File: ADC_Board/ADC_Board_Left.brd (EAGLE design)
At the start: 63.5 x 81.3 mm, 24 parts

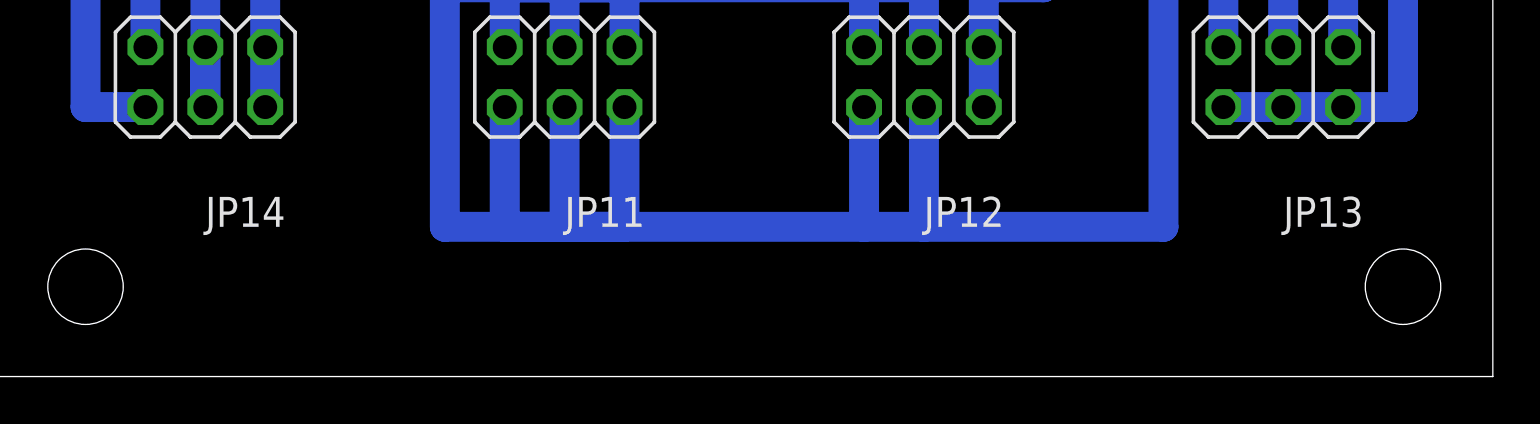
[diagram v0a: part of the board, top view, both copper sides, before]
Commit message: Alterações ligeiras nos esquemas eléctricos das placas das ADCs.
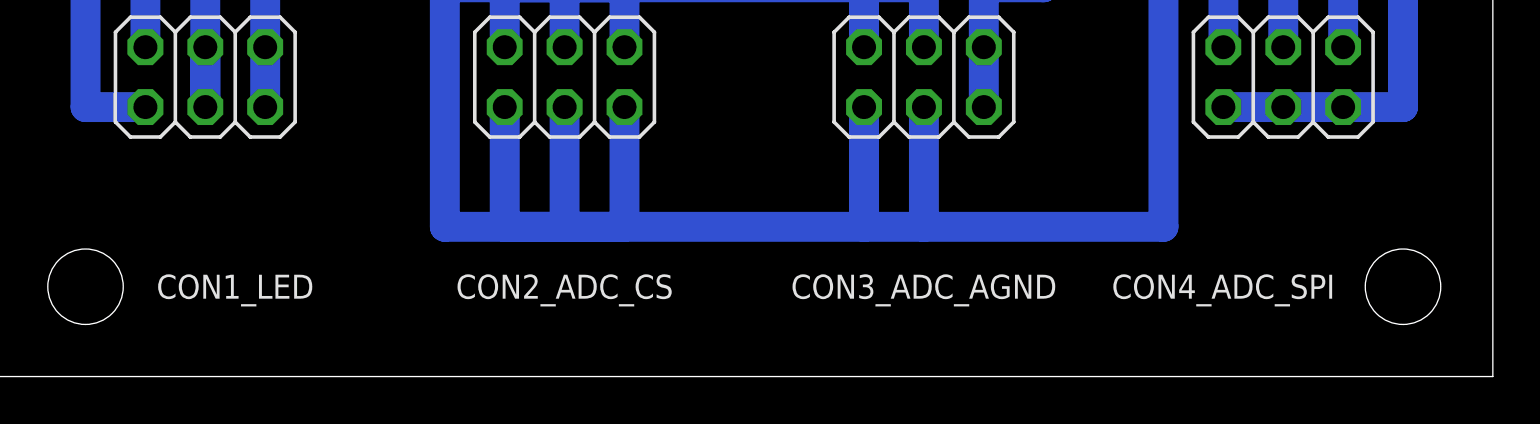
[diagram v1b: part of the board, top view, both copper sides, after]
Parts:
- renumbered JP11 to CON2_ADC_CS, JP12 to CON3_ADC_AGND, JP13 to CON4_ADC_SPI, JP14 to CON1_LED
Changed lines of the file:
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@@
 <wire x1="63.5" y1="-81.28" x2="0" y2="-81.28" width="0" layer="20"/>
 <text x="45.72" y="-12.7" size="1.778" layer="51">LEFT BOARD</text>
-<text x="-22.86" y="-12.7" size="1.778" layer="51">RIGHT CABLES</text>
+<text x="68.58" y="-12.7" size="1.778" layer="51">RIGHT CABLES</text>
 <text x="6.35" y="-64.77" size="1.016" layer="51" align="center">DI</text>
 <text x="6.35" y="-72.39" size="1.016" layer="51" align="center">DO</text>
@@
 <element name="JP9" library="pinhead" package="1X06" value="" x="29.21" y="-53.34" rot="R270"/>
 <element name="JP10" library="pinhead" package="1X06" value="" x="34.29" y="-53.34" rot="R270"/>
-<element name="JP11" library="pinhead" package="2X03" value="" x="24.13" y="-68.58" smashed="yes">
-<attribute name="NAME" x="24.13" y="-74.93" size="1.27" layer="25" ratio="10"/>
+<element name="CON2_ADC_CS" library="pinhead" package="2X03" value="" x="24.13" y="-68.58" smashed="yes">
+<attribute name="NAME" x="24.13" y="-77.47" size="1.016" layer="25" ratio="10" align="center"/>
 <attribute name="VALUE" x="20.32" y="-73.025" size="1.27" layer="27"/>
 </element>
-<element name="JP12" library="pinhead" package="2X03" value="" x="39.37" y="-68.58" smashed="yes">
-<attribute name="NAME" x="39.37" y="-74.93" size="1.27" layer="25" ratio="10"/>
+<element name="CON3_ADC_AGND" library="pinhead" package="2X03" value="" x="39.37" y="-68.58" smashed="yes">
+<attribute name="NAME" x="39.37" y="-77.47" size="1.016" layer="25" ratio="10" align="center"/>
 <attribute name="VALUE" x="35.56" y="-73.025" size="1.27" layer="27"/>
 </element>
-<element name="JP13" library="pinhead" package="2X03" value="" x="54.61" y="-68.58" smashed="yes">
-<attribute name="NAME" x="54.61" y="-74.93" size="1.27" layer="25" ratio="10"/>
+<element name="CON4_ADC_SPI" library="pinhead" package="2X03" value="" x="54.61" y="-68.58" smashed="yes">
+<attribute name="NAME" x="52.07" y="-77.47" size="1.016" layer="25" ratio="10" align="center"/>
 <attribute name="VALUE" x="50.8" y="-73.025" size="1.27" layer="27"/>
 </element>
-<element name="JP14" library="pinhead" package="2X03" value="" x="8.89" y="-68.58" smashed="yes">
-<attribute name="NAME" x="8.89" y="-74.93" size="1.27" layer="25" ratio="10"/>
+<element name="CON1_LED" library="pinhead" package="2X03" value="" x="8.89" y="-68.58" smashed="yes">
+<attribute name="NAME" x="10.16" y="-77.47" size="1.016" layer="25" ratio="10" align="center"/>
 <attribute name="VALUE" x="5.08" y="-73.025" size="1.27" layer="27"/>
 </element>
@@
 </signal>
 <signal name="GND">
-<contactref element="JP14" pad="5"/>
-<contactref element="JP14" pad="6"/>
+<contactref element="CON1_LED" pad="5"/>
+<contactref element="CON1_LED" pad="6"/>
 <wire x1="11.43" y1="-69.85" x2="11.43" y2="-67.31" width="1.27" layer="16"/>
 <wire x1="19.05" y1="-59.69" x2="11.43" y2="-59.69" width="1.27" layer="16"/>
@@
 <wire x1="13.97" y1="-49.53" x2="34.29" y2="-49.53" width="1.27" layer="16"/>
 <wire x1="8.89" y1="-49.53" x2="8.89" y2="-52.07" width="1.27" layer="16"/>
-<contactref element="JP14" pad="3"/>
-<contactref element="JP14" pad="4"/>
+<contactref element="CON1_LED" pad="3"/>
+<contactref element="CON1_LED" pad="4"/>
 <via x="8.89" y="-52.07" extent="1-16" drill="0.6" shape="square"/>
 <wire x1="8.89" y1="-52.07" x2="8.89" y2="-57.15" width="1.27" layer="1"/>
@@
 <wire x1="46.99" y1="-36.83" x2="52.07" y2="-36.83" width="1.27" layer="16"/>
 <wire x1="52.07" y1="-36.83" x2="52.07" y2="-67.31" width="1.27" layer="16"/>
-<contactref element="JP13" pad="2"/>
+<contactref element="CON4_ADC_SPI" pad="2"/>
 </signal>
 <signal name="SCK">
@@
 <wire x1="46.99" y1="-31.75" x2="57.15" y2="-31.75" width="1.27" layer="16"/>
 <wire x1="57.15" y1="-31.75" x2="57.15" y2="-67.31" width="1.27" layer="16"/>
-<contactref element="JP13" pad="6"/>
+<contactref element="CON4_ADC_SPI" pad="6"/>
 </signal>
 <signal name="MISO">
@@
 <wire x1="46.99" y1="-34.29" x2="54.61" y2="-34.29" width="1.27" layer="16"/>
 <wire x1="54.61" y1="-34.29" x2="54.61" y2="-67.31" width="1.27" layer="16"/>
-<contactref element="JP13" pad="4"/>
+<contactref element="CON4_ADC_SPI" pad="4"/>
 </signal>
 <signal name="V+">
@@
 <via x="13.97" y="-21.59" extent="1-16" drill="1" diameter="1.9304" shape="octagon"/>
 <wire x1="46.99" y1="-26.67" x2="52.07" y2="-26.67" width="1.27" layer="16"/>
-<contactref element="JP13" pad="5"/>
+<contactref element="CON4_ADC_SPI" pad="5"/>
 <wire x1="52.07" y1="-26.67" x2="59.69" y2="-26.67" width="1.27" layer="16"/>
 <wire x1="59.69" y1="-26.67" x2="59.69" y2="-69.85" width="1.27" layer="16"/>
 <wire x1="59.69" y1="-69.85" x2="57.15" y2="-69.85" width="1.27" layer="16"/>
 <contactref element="C1" pad="1"/>
-<contactref element="JP13" pad="3"/>
+<contactref element="CON4_ADC_SPI" pad="3"/>
 <wire x1="57.15" y1="-69.85" x2="54.61" y2="-69.85" width="1.27" layer="16"/>
-<contactref element="JP13" pad="1"/>
+<contactref element="CON4_ADC_SPI" pad="1"/>
 <wire x1="54.61" y1="-69.85" x2="52.07" y2="-69.85" width="1.27" layer="16"/>
 <wire x1="13.97" y1="-21.59" x2="52.07" y2="-21.59" width="1.27" layer="1"/>
@@
 <wire x1="46.99" y1="-29.21" x2="44.45" y2="-29.21" width="1.27" layer="16"/>
 <wire x1="44.45" y1="-41.91" x2="46.99" y2="-41.91" width="1.27" layer="16"/>
-<contactref element="JP12" pad="6"/>
+<contactref element="CON3_ADC_AGND" pad="6"/>
 <wire x1="41.91" y1="-67.31" x2="41.91" y2="-64.77" width="1.27" layer="16"/>
 <wire x1="41.91" y1="-64.77" x2="44.45" y2="-64.77" width="1.27" layer="16"/>
 <wire x1="44.45" y1="-64.77" x2="44.45" y2="-57.15" width="1.27" layer="16"/>
 <contactref element="C1" pad="2"/>
-<contactref element="JP12" pad="5"/>
+<contactref element="CON3_ADC_AGND" pad="5"/>
 <wire x1="41.91" y1="-67.31" x2="41.91" y2="-69.85" width="1.27" layer="16"/>
 <contactref element="JP10" pad="5"/>
@@
 <wire x1="13.97" y1="-11.43" x2="3.81" y2="-11.43" width="1.27" layer="16"/>
 <wire x1="3.81" y1="-11.43" x2="3.81" y2="-69.85" width="1.27" layer="16"/>
-<contactref element="JP14" pad="1"/>
+<contactref element="CON1_LED" pad="1"/>
 <wire x1="3.81" y1="-69.85" x2="6.35" y2="-69.85" width="1.27" layer="16"/>
 </signal>
@@
 <wire x1="13.97" y1="-54.61" x2="6.35" y2="-54.61" width="1.27" layer="16"/>
 <wire x1="6.35" y1="-67.31" x2="6.35" y2="-54.61" width="1.27" layer="16"/>
-<contactref element="JP14" pad="2"/>
+<contactref element="CON1_LED" pad="2"/>
 </signal>
 <signal name="CS">
@@
 <wire x1="49.53" y1="-39.37" x2="49.53" y2="-74.93" width="1.27" layer="16"/>
 <wire x1="49.53" y1="-74.93" x2="39.37" y2="-74.93" width="1.27" layer="16"/>
-<contactref element="JP11" pad="1"/>
-<contactref element="JP11" pad="3"/>
-<contactref element="JP11" pad="5"/>
-<contactref element="JP11" pad="2"/>
-<contactref element="JP11" pad="4"/>
-<contactref element="JP11" pad="6"/>
-<contactref element="JP12" pad="1"/>
-<contactref element="JP12" pad="3"/>
-<contactref element="JP12" pad="2"/>
-<contactref element="JP12" pad="4"/>
+<contactref element="CON2_ADC_CS" pad="1"/>
+<contactref element="CON2_ADC_CS" pad="3"/>
+<contactref element="CON2_ADC_CS" pad="5"/>
+<contactref element="CON2_ADC_CS" pad="2"/>
+<contactref element="CON2_ADC_CS" pad="4"/>
+<contactref element="CON2_ADC_CS" pad="6"/>
+<contactref element="CON3_ADC_AGND" pad="1"/>
+<contactref element="CON3_ADC_AGND" pad="3"/>
+<contactref element="CON3_ADC_AGND" pad="2"/>
+<contactref element="CON3_ADC_AGND" pad="4"/>
 <wire x1="39.37" y1="-74.93" x2="36.83" y2="-74.93" width="1.27" layer="16"/>
 <wire x1="19.05" y1="-74.93" x2="24.13" y2="-74.93" width="1.27" layer="16"/>
